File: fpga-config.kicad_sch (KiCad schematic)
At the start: 16 parts, among them J2 Tag-Connect_TC2030-IDC-NL_2x3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, U1 MPFS250T-FCVG484, U3 MT25QL01GBBB1EW9-0SIT

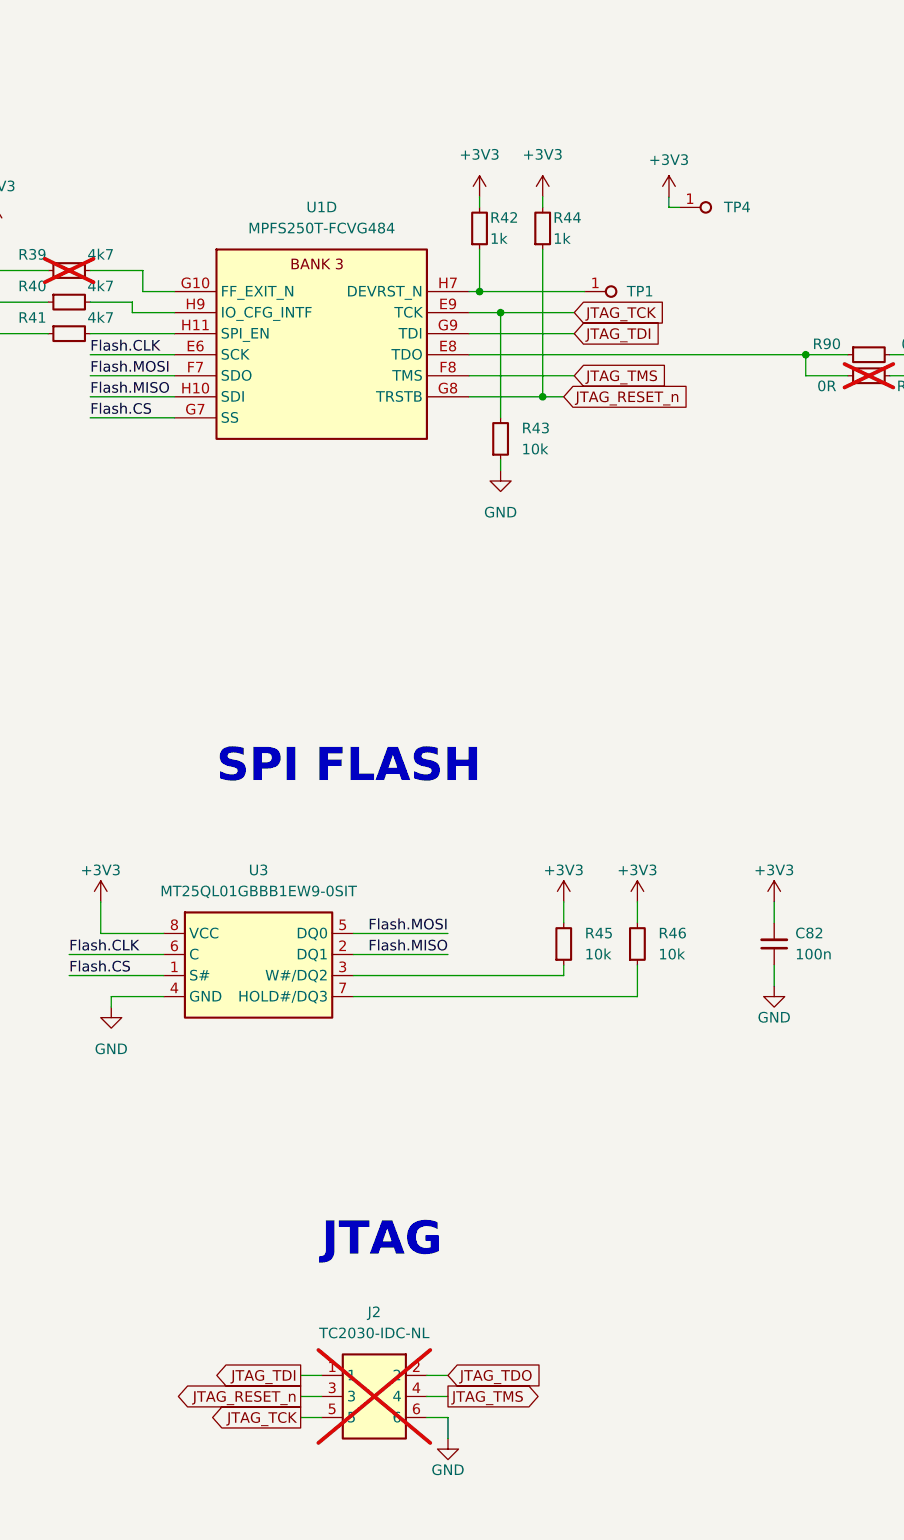
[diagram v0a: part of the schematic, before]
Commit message: [#59910] Change Tag-Connect to 10 pin
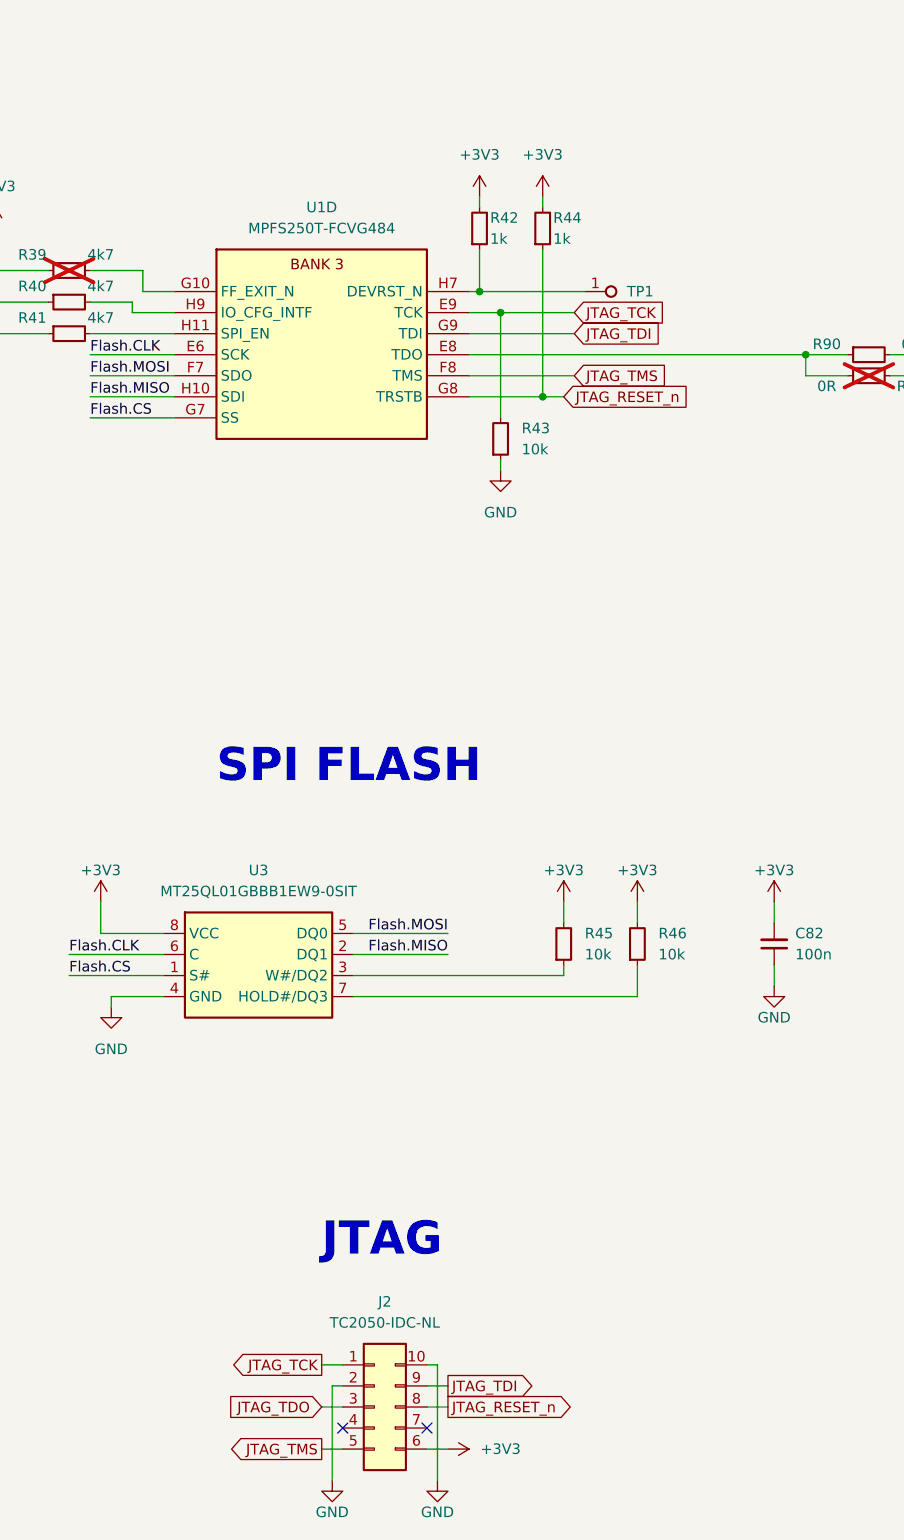
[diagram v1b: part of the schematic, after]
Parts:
- removed J2: Tag-Connect_TC2030-IDC-NL_2x3_P1.27mm, antmicro-footprints:Tag-Connect_TC2030-IDC-NL_2x3_P1.27mm, symbol antmicroTestPoints:Tag-Connect_TC2030-IDC-NL_2x3_P1.27mm
- removed TP4: TP_0.75mm_SMD, antmicro-footprints:TP_SMD_0.75mm, symbol antmicroTestPoints:TP_0.75mm_SMD
- added J2: Tag-Connect_TC2050-IDC-NL_2x5_P1.27mm, antmicro-footprints:Tag-Connect_TC2050-IDC-NL_2x5_P1.27mm, symbol antmicroTestPoints:Tag-Connect_TC2050-IDC-NL_2x5_P1.27mm
- TP1: Public (none) -> False
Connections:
- net +3V3: now also J2.6
- net GND: now also J2.10, J2.2
- net JTAG_RESET_n: now also J2.8
- net JTAG_TCK: now also J2.1
- net JTAG_TDI: now also J2.9
- net JTAG_TDO: now also J2.3
- net JTAG_TMS: now also J2.5
- no-connect marks 0 -> 2

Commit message: [#60905] Add DNP attribute to Tag-Connect
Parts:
- J2: DNP (none) -> DNP; now not fitted
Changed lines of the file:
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@@
   )
   (symbol (lib_id "antmicroTestPoints:Tag-Connect_TC2050-IDC-NL_2x5_P1.27mm") (at 200.66 215.9 0) (unit 1)
-    (in_bom no) (on_board yes) (dnp no) (fields_autoplaced)
+    (in_bom no) (on_board yes) (dnp yes) (fields_autoplaced)
     (property "Reference" "J2" (at 205.74 208.28 0)
       (effects (font (size 1.27 1.27) (thickness 0.15)))
@@
       (effects (font (size 1.27 1.27) (thickness 0.15)) (justify left bottom) hide)
     )
+    (property "DNP" "DNP" (at 200.66 215.9 0)
+      (effects (font (size 1.27 1.27)) hide)
+    )
     (pin "1")

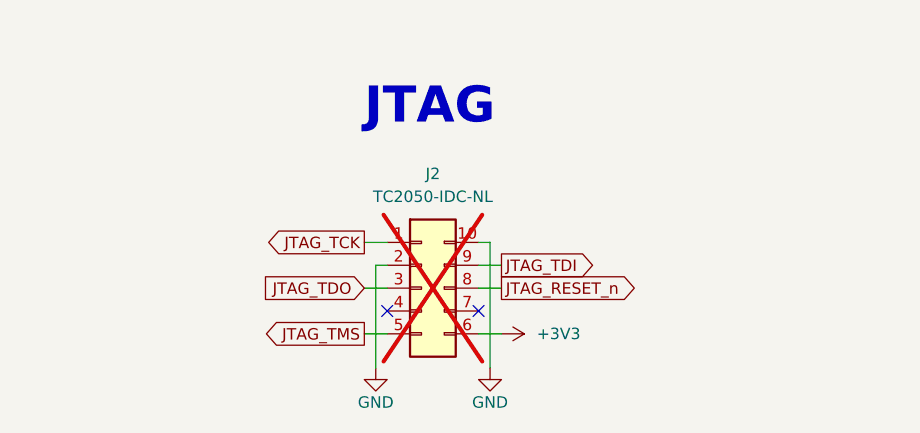
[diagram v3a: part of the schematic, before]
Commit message: [#73079] Update symbols, clean ERC
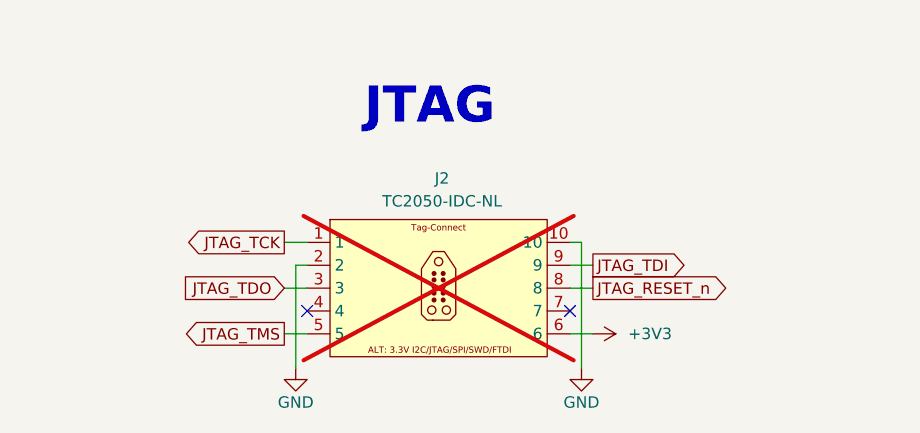
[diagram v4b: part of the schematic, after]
